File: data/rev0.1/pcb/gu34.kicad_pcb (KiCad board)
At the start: 2 copper layers, 247.2 x 114.5 mm, 69 parts, among them SW1 SW_PUSH, SW10 SW_PUSH, SW11 SW_PUSH, SW12 SW_PUSH, SW13 SW_PUSH, SW14 SW_PUSH, SW15 SW_PUSH, SW16 SW_PUSH, SW17 SW_PUSH, SW18 SW_PUSH, SW19 SW_PUSH, SW2 SW_PUSH, SW20 SW_PUSH, SW21 SW_PUSH, SW22 SW_PUSH, SW23 SW_PUSH, SW24 SW_PUSH, SW25 SW_PUSH, SW26 SW_PUSH, SW27 SW_PUSH, SW28 SW_PUSH, SW29 SW_PUSH, SW3 SW_PUSH, SW30 SW_PUSH, SW31 SW_PUSH, SW32 SW_PUSH, SW33 SW_PUSH, SW34 SW_PUSH, SW4 SW_PUSH, SW5 SW_PUSH, SW6 SW_PUSH, SW7 SW_PUSH, SW8 SW_PUSH, SW9 SW_PUSH

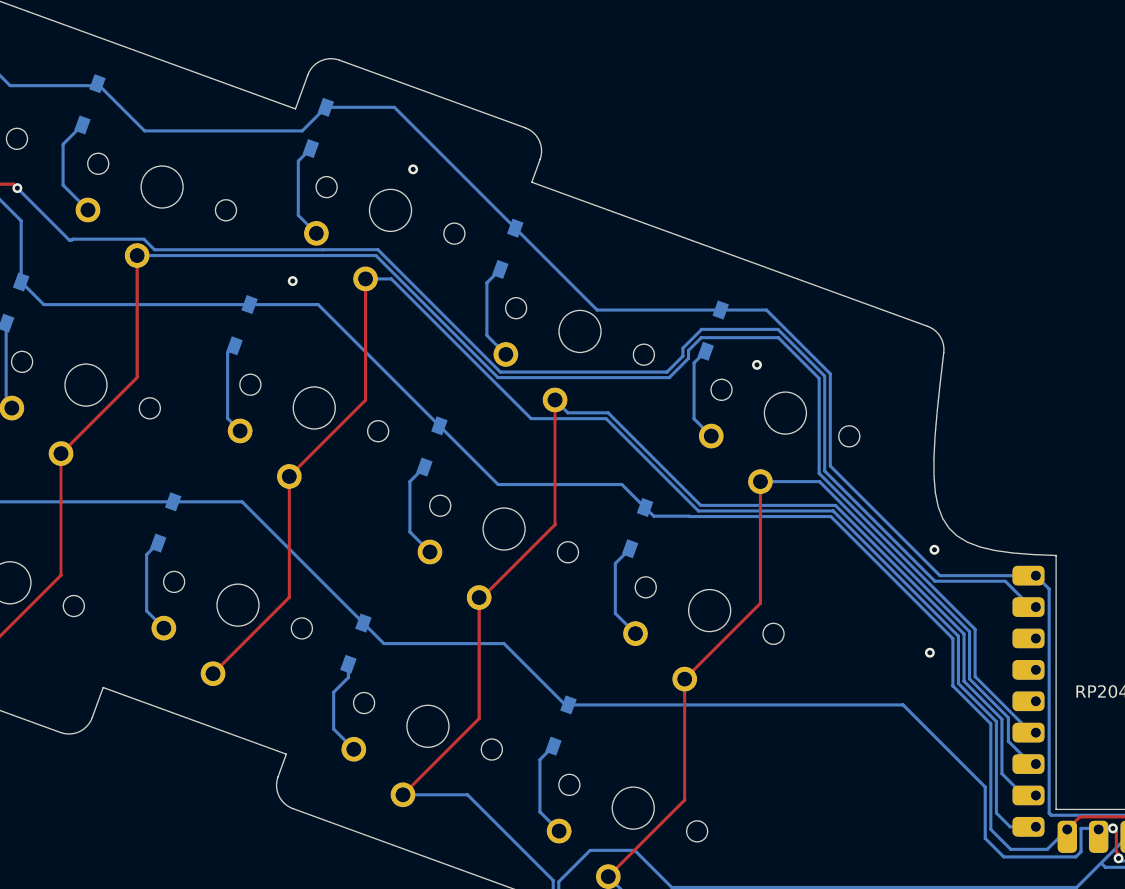
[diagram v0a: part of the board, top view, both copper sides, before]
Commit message: rp2040 zero のフットプリントとシンボルが正しくなかったため、修正した
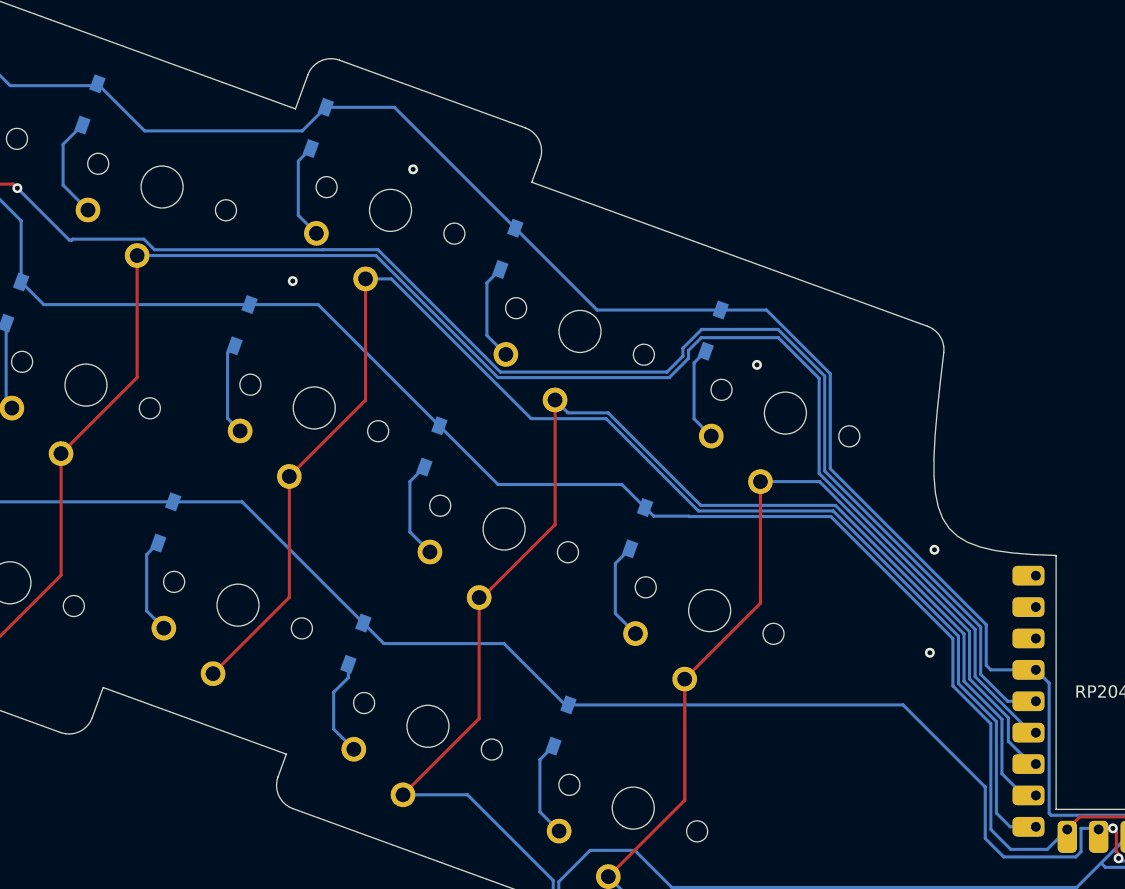
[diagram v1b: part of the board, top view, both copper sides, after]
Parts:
- removed De: D, gu36:Diode_SMD
- added D2: D, gu34:Diode_SMD, F.Cu at (58.1, 29.0)
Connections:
- RZ1 pad 19: row0 -> col0
- RZ1 pad 20: col0 -> row0
- RZ1 pad 22: VCC -> GND
- RZ1 pad 23: GND -> VCC
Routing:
- net col0: track 163.4 -> 168.8 mm
- net row0: track 272.7 -> 270.3 mm
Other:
- board text added: "JLCJLCJLCJLC"
- board text added: "gu34 rev0.1"
